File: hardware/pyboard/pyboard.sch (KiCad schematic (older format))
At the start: 71 parts, among them J1 Battery, J10 P9-P10, J2 Y1-Y8, J3 X9-X16, J4 USB_B_Micro, J5 P1-P8, J6 X17-X24, J7 Y9-Y16, J8 X1-X8, J9 Micro_SD_Card_Det, Q1 DMP2165UW, Q2 IRLML6402, SW1 RST, SW2 USR, U1 STM32F405RGT6, U2 MCP1703A-3302_SOT89, U3 TPS2051BDBV, U4 MMA7660FC, Y1 32.768kHz, Y2 12MHz

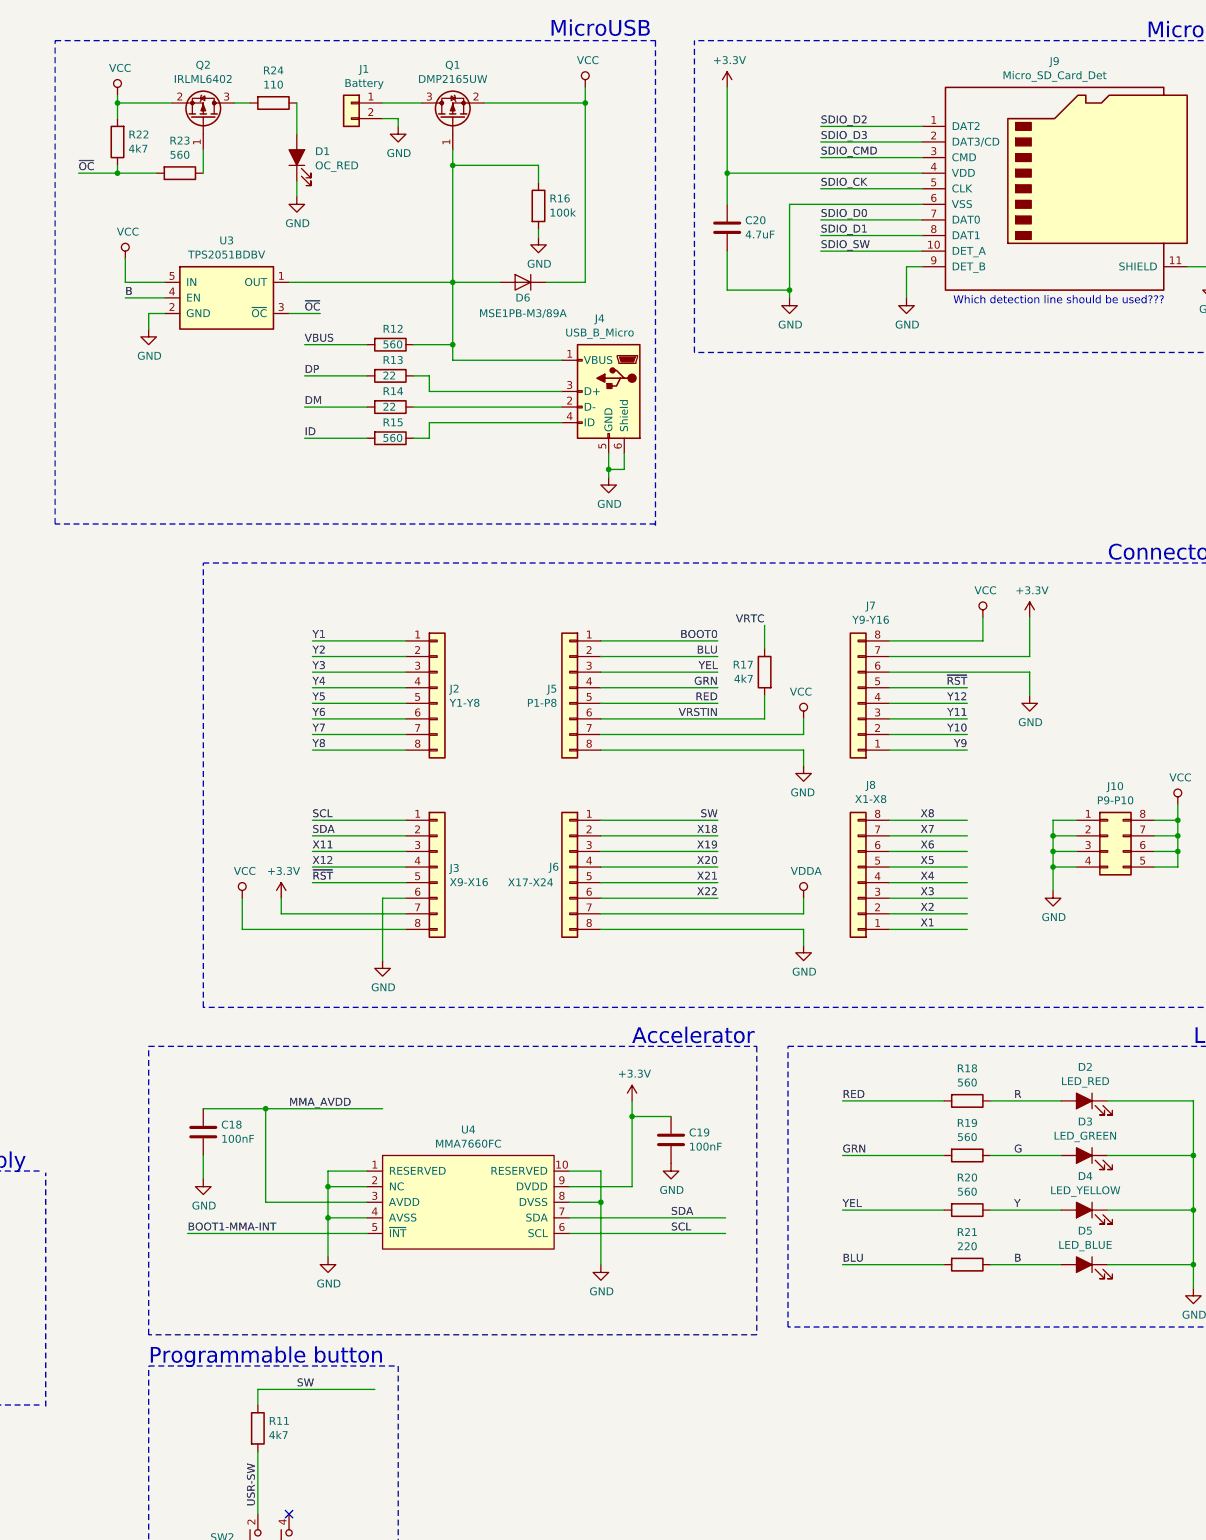
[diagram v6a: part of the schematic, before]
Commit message: Add footprint for micro usb
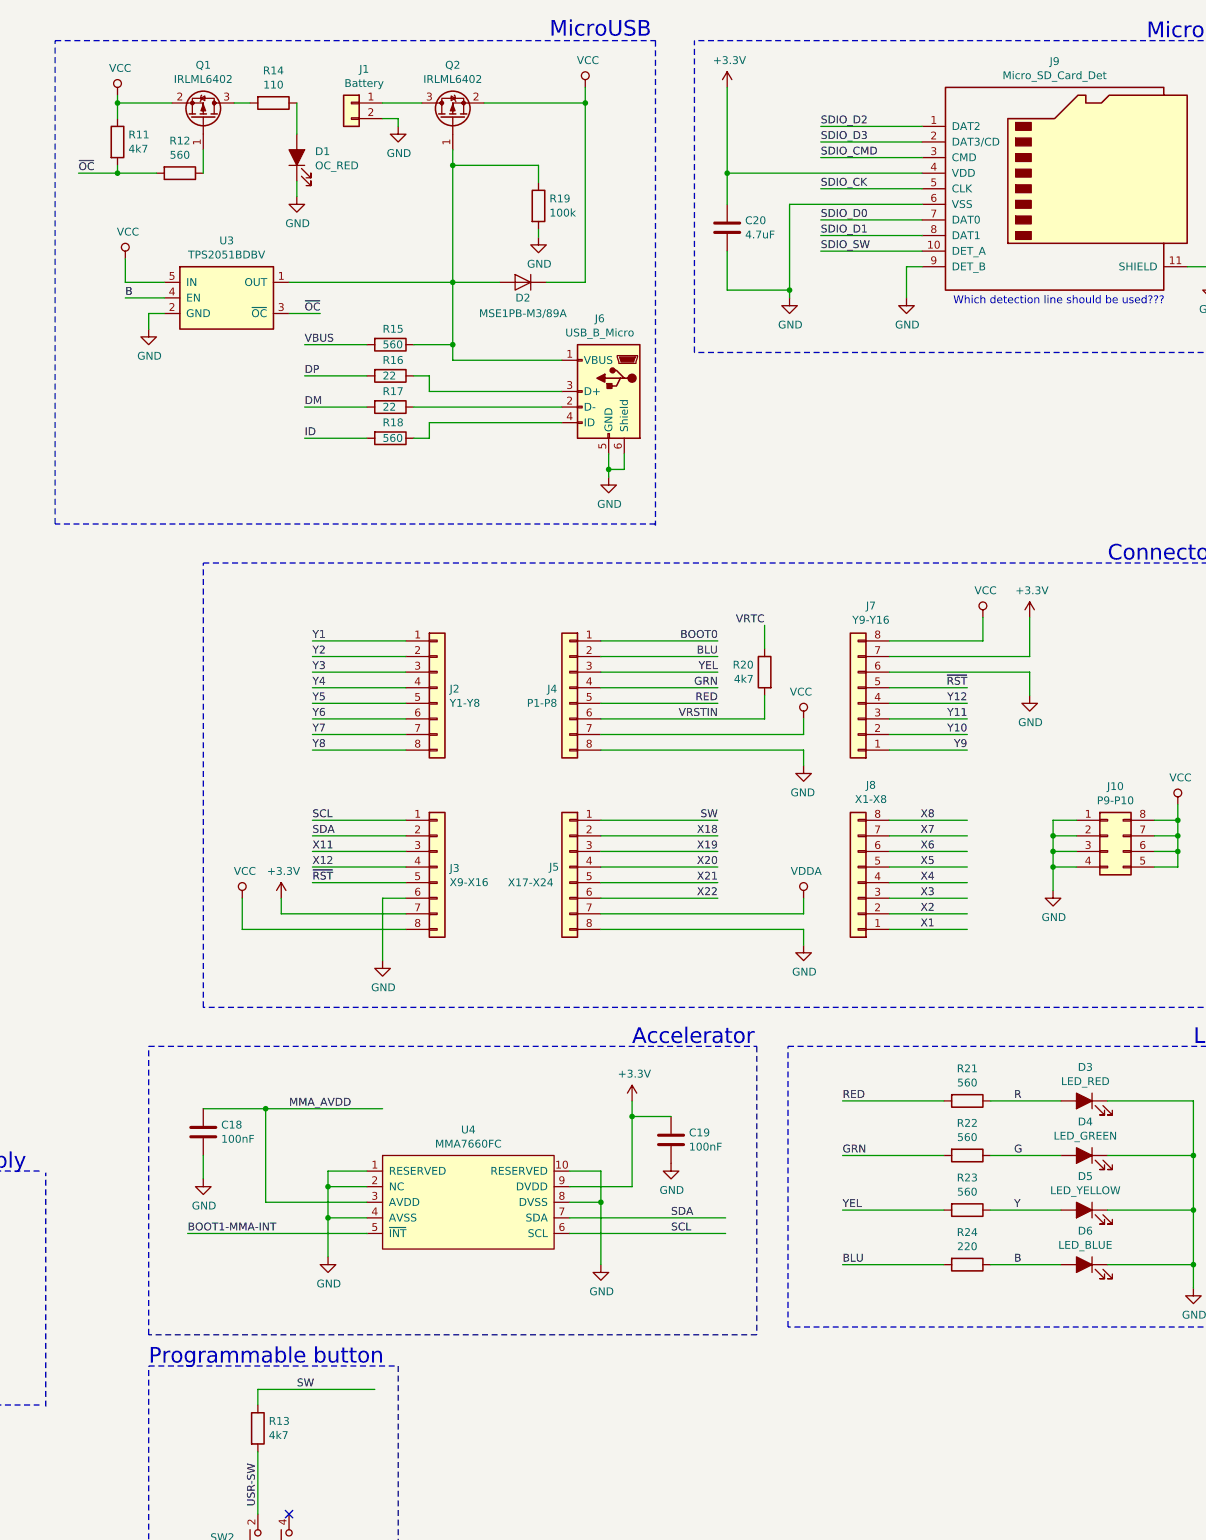
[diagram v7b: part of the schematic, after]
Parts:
- removed Q1: DMP2165UW, symbol components:DMP2165UW
- removed R22: 4k7, symbol Device:R
- added Q2: IRLML6402, Package_TO_SOT_SMD:SOT-23, symbol Transistor_FET:IRLML6402
- added R11: 4k7, Resistor_SMD:R_0603_1608Metric, symbol Device:R
- J6: renamed from J4; footprint (none) -> components:USB_Micro-B_10118192-0001LF
- R14: renamed from R24; footprint (none) -> Resistor_SMD:R_0603_1608Metric
- renumbered D6 to D2, D2 to D3, D3 to D4, D4 to D5, D5 to D6, J5 to J4, J6 to J5, Q2 to Q1, R23 to R12, R11 to R13, R12 to R15, R13 to R16, R14 to R17, R15 to R18, R16 to R19, R17 to R20, R18 to R21, R19 to R22, R20 to R23, R21 to R24

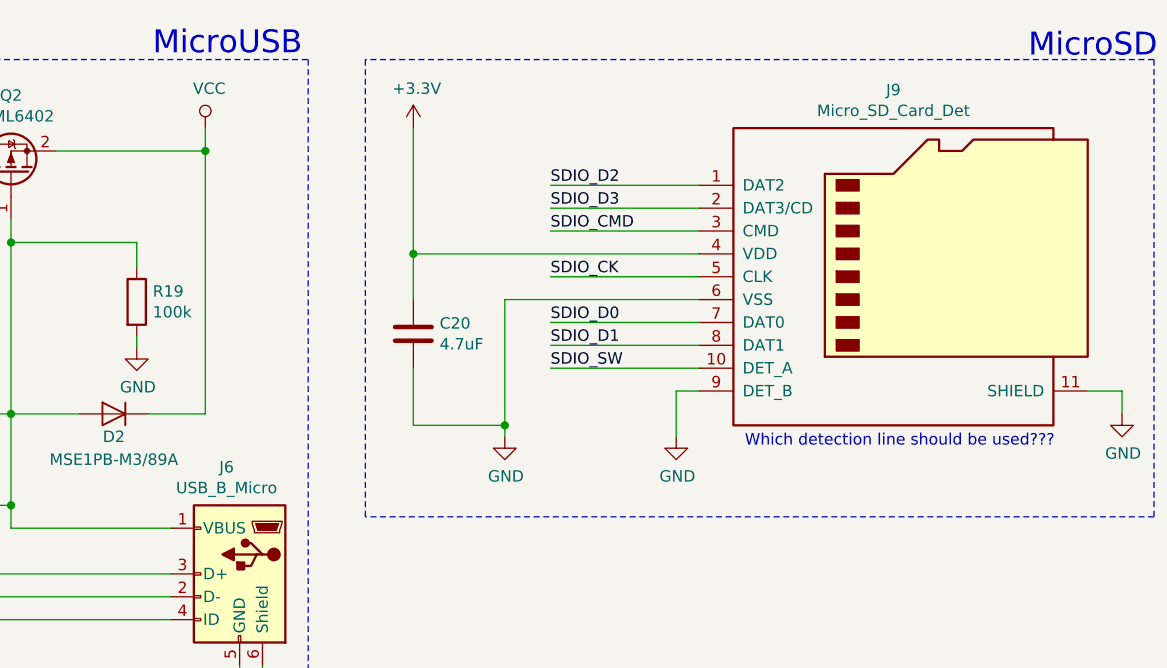
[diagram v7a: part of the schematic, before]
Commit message: Add footprint for microSD card
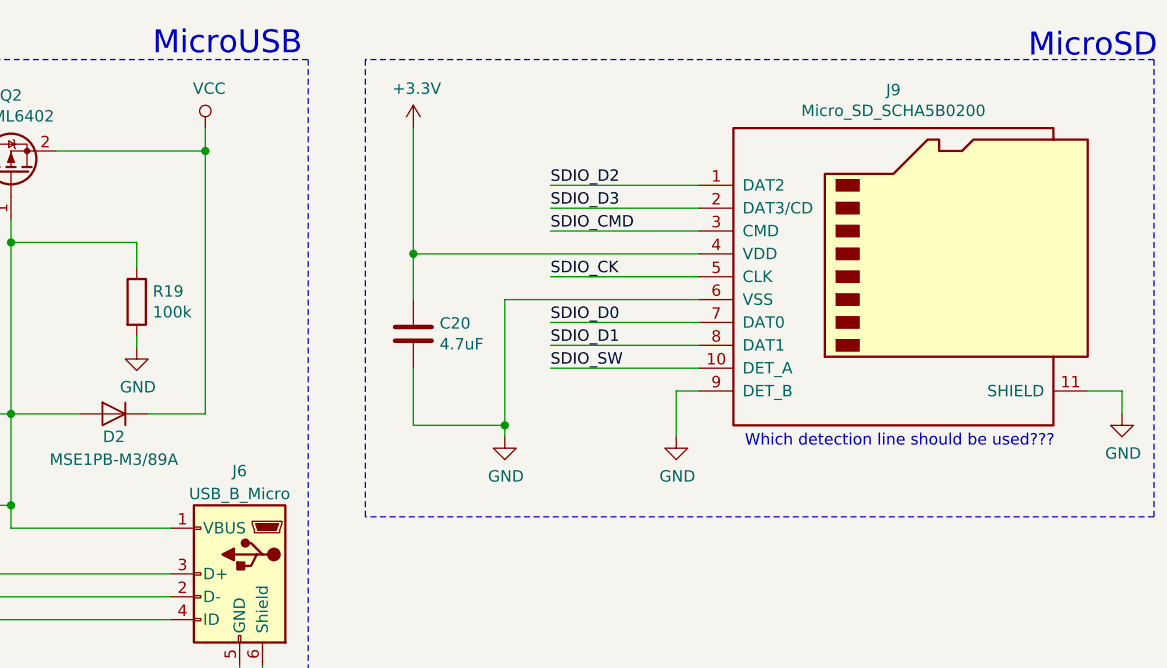
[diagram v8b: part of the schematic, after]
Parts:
- J9: value Micro_SD_Card_Det -> Micro_SD_SCHA5B0200; footprint (none) -> components:microSD_HC_SCHA5B0200
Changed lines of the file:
@@
 U 1 1 5D8179A9
 P 11750 3000
-F 0 "J6" H 11807 3467 50  0000 C CNN
-F 1 "USB_B_Micro" H 11807 3376 50  0000 C CNN
+F 0 "J6" H 11750 3450 50  0000 C CNN
+F 1 "USB_B_Micro" H 11750 3350 50  0000 C CNN
 F 2 "components:USB_Micro-B_10118192-0001LF" H 11900 2950 50  0001 C CNN
-F 3 "~" H 11900 2950 50  0001 C CNN
+F 3 "https://belchip.by/sitedocs/34170.pdf" H 11900 2950 50  0001 C CNN
 	1    11750 3000
 	-1   0    0    -1
@@
 P 14660 1700
 F 0 "J9" H 14610 2517 50  0000 C CNN
-F 1 "Micro_SD_Card_Det" H 14610 2426 50  0000 C CNN
-F 2 "" H 16710 2400 50  0001 C CNN
-F 3 "https://www.hirose.com/product/en/download_file/key_name/DM3/category/Catalog/doc_file_id/49662/?file_category_id=4&item_id=195&is_series=1" H 14660 1800 50  0001 C CNN
+F 1 "Micro_SD_SCHA5B0200" H 14610 2426 50  0000 C CNN
+F 2 "components:microSD_HC_SCHA5B0200" H 16710 2400 50  0001 C CNN
+F 3 "https://belchip.by/product/?selected_product=04939" H 14660 1800 50  0001 C CNN
 	1    14660 1700
 	1    0    0    -1
@@
 	1    0    0    -1
 $EndComp
-Text Notes 13960 2450 0    50   ~ 0
-Which detection line should be used???\n
 Wire Wire Line
 	13760 2100 13110 2100
@@
 	1    0    0    -1
 $EndComp
+Text Notes 13960 2450 0    50   ~ 0
+Which detection line should be used???\n
 $EndSCHEMATC
